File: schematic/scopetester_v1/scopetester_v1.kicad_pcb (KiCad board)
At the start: 2 copper layers, 73.7 x 54.4 mm, 42 parts, among them J1 CON_PWR, J2 Conn_01x04, J3 AVR_ISP, SW1 SW_Push, U1 ATmega8A-P, Y1 12MHz

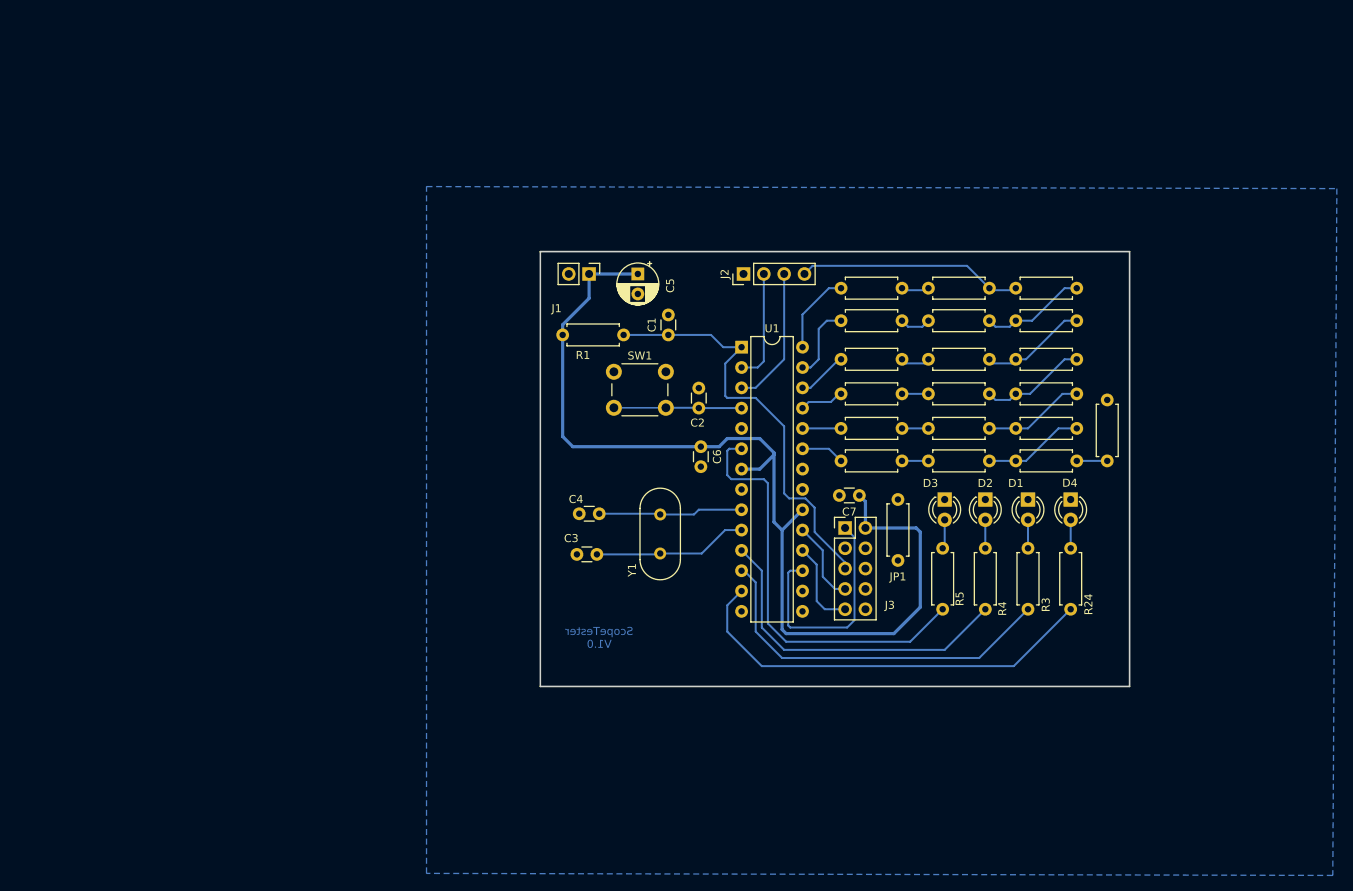
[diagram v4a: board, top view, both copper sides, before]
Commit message: Finalized PCB layout (edition 1)
The DRC error of 'mission connection between items' was solved using a
phony track on the front side. This is just to satisfy KiCad because it
does not seem to understand that jumper is actually bridged.
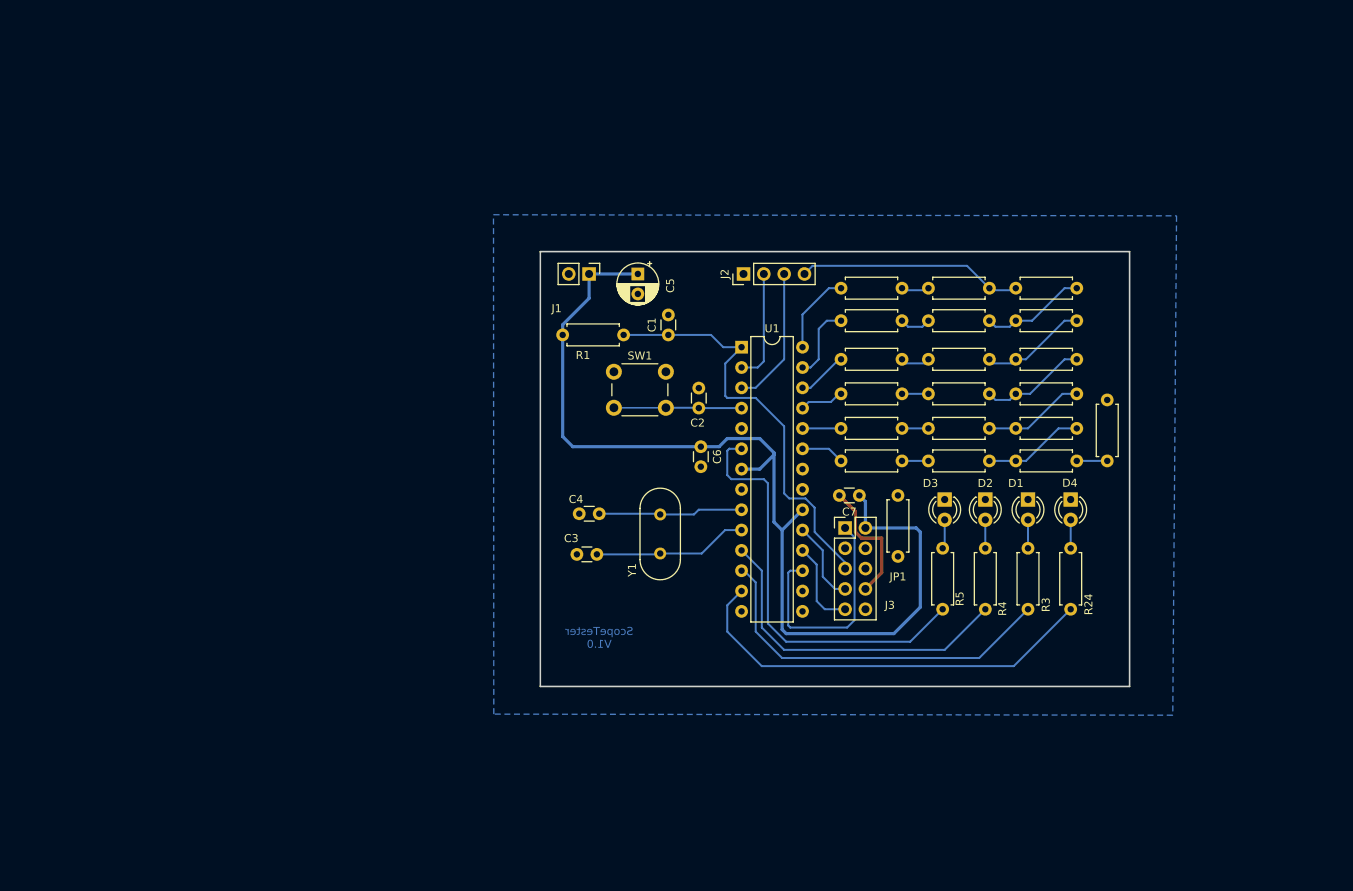
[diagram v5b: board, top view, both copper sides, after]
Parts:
- moved JP1 0.51 mm to (130.8, 97.5)
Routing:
- net GND: track 0.00 -> 16.2 mm
- net ANG_OUT_0: track 28.2 -> 27.5 mm
- net Net-(R11-Pad1): track 3.51 -> 2.79 mm

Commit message: Now using 16MHz clock instead of 12MHz
This increases the waveform frequencies by 33.3%.
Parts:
- Y1: value 12MHz -> 16MHz
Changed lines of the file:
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@@
       (effects (font (size 1 1) (thickness 0.15)))
     )
-    (fp_text value "12MHz" (at 2.44 3.525 90) (layer "F.Fab")
+    (fp_text value "16MHz" (at 2.44 3.525 90) (layer "F.Fab")
       (effects (font (size 1 1) (thickness 0.15)))
     )
